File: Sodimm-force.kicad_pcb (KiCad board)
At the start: 2 copper layers, 71.6 x 71.6 mm, 1 part

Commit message: Схема закончена, часть компонентов расставлена на плате
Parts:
- removed G***: LOGO, LOGO
- added C1: 22uF, Capacitor_SMD:C_0402_1005Metric, F.Cu at (151.9, 58.5)
- added C10: 22uF, Capacitor_SMD:C_0402_1005Metric, F.Cu at (154.8, 64.4)
- added C11: 22uF, Capacitor_SMD:C_0402_1005Metric, F.Cu at (154.8, 66.4)
- added C12: 22uF, Capacitor_SMD:C_0402_1005Metric, F.Cu at (154.8, 68.3)
- added C13: 100nF, Capacitor_SMD:C_0402_1005Metric, F.Cu at (157.7, 58.5)
- added C14: 100nF, Capacitor_SMD:C_0402_1005Metric, F.Cu at (157.7, 60.5)
- added C15: 100nF, Capacitor_SMD:C_0402_1005Metric, F.Cu at (157.7, 62.4)
- added C16: 100nF, Capacitor_SMD:C_0402_1005Metric, F.Cu at (157.7, 64.4)
- added C17: 100nF, Capacitor_SMD:C_0402_1005Metric, F.Cu at (157.7, 66.4)
- added C18: 100nF, Capacitor_SMD:C_0402_1005Metric, F.Cu at (157.7, 68.3)
- added C19: 22uF, Capacitor_SMD:C_0402_1005Metric, F.Cu at (160.5, 58.5)
- added C2: 22uF, Capacitor_SMD:C_0402_1005Metric, F.Cu at (151.9, 60.5)
- added C20: 22uF, Capacitor_SMD:C_0402_1005Metric, F.Cu at (160.5, 60.5)
- added C21: 22uF, Capacitor_SMD:C_0402_1005Metric, F.Cu at (160.5, 62.4)
- added C22: 22uF, Capacitor_SMD:C_0402_1005Metric, F.Cu at (160.5, 64.4)
- added C23: 100nF, Capacitor_SMD:C_0402_1005Metric, F.Cu at (138.8, 74.5)
- added C24: 100nF, Capacitor_SMD:C_0402_1005Metric, F.Cu at (138.8, 76.5)
- added C25: 10uF, Capacitor_SMD:C_0402_1005Metric, F.Cu at (138.8, 78.5)
- added C26: 100nF, Capacitor_SMD:C_0402_1005Metric, F.Cu at (138.8, 80.4)
- added C27: 2.2uF, Capacitor_SMD:C_0402_1005Metric, F.Cu at (138.8, 82.4)
- added C28: 100nF, Capacitor_SMD:C_0402_1005Metric, F.Cu at (138.8, 84.4)
- added C29: 10uF, Capacitor_SMD:C_0402_1005Metric, F.Cu at (138.8, 86.3)
- added C3: 22uF, Capacitor_SMD:C_0402_1005Metric, F.Cu at (151.9, 62.4)
- added C30: 2.2uF, Capacitor_SMD:C_0402_1005Metric, F.Cu at (141.6, 74.5)
- added C31: 1nF, Capacitor_SMD:C_0402_1005Metric, F.Cu at (141.6, 76.5)
- added C32: 100nF, Capacitor_SMD:C_0402_1005Metric, F.Cu at (141.6, 78.5)
- added C33: 22uF, Capacitor_SMD:C_0402_1005Metric, F.Cu at (141.6, 80.4)
- added C34: 2.2uF, Capacitor_SMD:C_0402_1005Metric, F.Cu at (141.6, 82.4)
- added C35: 12p, Capacitor_SMD:C_0402_1005Metric, F.Cu at (141.6, 84.4)
- added C36: 2.2uF, Capacitor_SMD:C_0402_1005Metric, F.Cu at (141.6, 86.3)
- added C37: 220nF, Capacitor_SMD:C_0402_1005Metric, F.Cu at (144.5, 74.5)
- added C38: 22uF, Capacitor_SMD:C_0402_1005Metric, F.Cu at (144.5, 76.5)
- added C39: 220nF, Capacitor_SMD:C_0402_1005Metric, F.Cu at (144.5, 78.5)
- added C4: 22uF, Capacitor_SMD:C_0402_1005Metric, F.Cu at (151.9, 64.4)
- added C40: 2.2uF, Capacitor_SMD:C_0402_1005Metric, F.Cu at (144.5, 80.4)
- added C41: 22uF, Capacitor_SMD:C_0402_1005Metric, F.Cu at (144.5, 82.4)
- added C42: 12p, Capacitor_SMD:C_0402_1005Metric, F.Cu at (144.5, 84.4)
- added C43: 2.2uF, Capacitor_SMD:C_0402_1005Metric, F.Cu at (144.5, 86.3)
- added C44: 22uF, Capacitor_SMD:C_0402_1005Metric, F.Cu at (147.4, 74.5)
- added C45: 2.2uF, Capacitor_SMD:C_0402_1005Metric, F.Cu at (147.4, 76.5)
- added C46: 220nF, Capacitor_SMD:C_0402_1005Metric, F.Cu at (147.4, 78.5)
- added C47: 22uF, Capacitor_SMD:C_0402_1005Metric, F.Cu at (147.4, 80.4)
- added C48: 2.2uF, Capacitor_SMD:C_0402_1005Metric, F.Cu at (147.4, 82.4)
- added C49: 22uF, Capacitor_SMD:C_0402_1005Metric, F.Cu at (147.4, 84.4)
- added C5: 22uF, Capacitor_SMD:C_0402_1005Metric, F.Cu at (151.9, 66.4)
- added C50: 1uF, Capacitor_SMD:C_0402_1005Metric, F.Cu at (147.4, 86.3)
- added C51: 2.2uF, Capacitor_SMD:C_0402_1005Metric, F.Cu at (150.3, 74.5)
- added C52: 10uF, Capacitor_SMD:C_0402_1005Metric, F.Cu at (150.3, 76.5)
- added C53: 22uF, Capacitor_SMD:C_0402_1005Metric, F.Cu at (150.3, 78.5)
- added C54: 2.2uF, Capacitor_SMD:C_0402_1005Metric, F.Cu at (150.3, 80.4)
- added C55: 22uF, Capacitor_SMD:C_0402_1005Metric, F.Cu at (150.3, 82.4)
- added C56: 2.2uF, Capacitor_SMD:C_0402_1005Metric, F.Cu at (150.3, 84.4)
- added C57: 1uF, Capacitor_SMD:C_0402_1005Metric, F.Cu at (150.3, 86.3)
- added C58: 2.2uF, Capacitor_SMD:C_0402_1005Metric, F.Cu at (153.1, 74.5)
- added C59: 1uF, Capacitor_SMD:C_0402_1005Metric, F.Cu at (153.1, 76.5)
- added C6: 22uF, Capacitor_SMD:C_0402_1005Metric, F.Cu at (151.9, 68.3)
- added C60: 2.2uF, Capacitor_SMD:C_0402_1005Metric, F.Cu at (153.1, 78.5)
- added C61: 100nF, Capacitor_SMD:C_0402_1005Metric, F.Cu at (153.1, 80.4)
- added C62: 2.2uF, Capacitor_SMD:C_0402_1005Metric, F.Cu at (153.1, 82.4)
- added C63: 1uF, Capacitor_SMD:C_0402_1005Metric, F.Cu at (153.1, 84.4)
- added C64: 22uF, Capacitor_SMD:C_0402_1005Metric, F.Cu at (105.4, 88.0)
- added C65: 2.2uF, Capacitor_SMD:C_0402_1005Metric, F.Cu at (105.4, 89.9)
- added C66: 2.2uF, Capacitor_SMD:C_0402_1005Metric, F.Cu at (105.4, 91.9)
- added C67: 2.2uF, Capacitor_SMD:C_0402_1005Metric, F.Cu at (105.4, 93.9)
- added C68: 1uF, Capacitor_SMD:C_0402_1005Metric, F.Cu at (105.4, 95.9)
- added C69: 1uF, Capacitor_SMD:C_0402_1005Metric, F.Cu at (105.4, 97.8)
- added C7: 22uF, Capacitor_SMD:C_0402_1005Metric, F.Cu at (154.8, 58.5)
- added C70: 100nF, Capacitor_SMD:C_0402_1005Metric, F.Cu at (105.4, 99.8)
- added C71: 100nF, Capacitor_SMD:C_0402_1005Metric, F.Cu at (108.3, 88.0)
- added C72: 100nF, Capacitor_SMD:C_0402_1005Metric, F.Cu at (108.3, 89.9)
- added C73: 100nF, Capacitor_SMD:C_0402_1005Metric, F.Cu at (108.3, 91.9)
- added C74: 1uF, Capacitor_SMD:C_0402_1005Metric, F.Cu at (108.3, 93.9)
- added C75: 1uF, Capacitor_SMD:C_0402_1005Metric, F.Cu at (108.3, 95.9)
- added C76: 1uF, Capacitor_SMD:C_0402_1005Metric, F.Cu at (108.3, 97.8)
- added C77: 100nF, Capacitor_SMD:C_0402_1005Metric, F.Cu at (108.3, 99.8)
- added C78: 100nF, Capacitor_SMD:C_0402_1005Metric, F.Cu at (111.1, 88.0)
- added C79: 100nF, Capacitor_SMD:C_0402_1005Metric, F.Cu at (111.1, 89.9)
- added C8: 22uF, Capacitor_SMD:C_0402_1005Metric, F.Cu at (154.8, 60.5)
- added C80: 100nF, Capacitor_SMD:C_0402_1005Metric, F.Cu at (111.1, 91.9)
- added C81: 1uF, Capacitor_SMD:C_0402_1005Metric, F.Cu at (111.1, 93.9)
- added C82: 1uF, Capacitor_SMD:C_0402_1005Metric, F.Cu at (111.1, 95.9)
- added C83: 1uF, Capacitor_SMD:C_0402_1005Metric, F.Cu at (111.1, 97.8)
- added C84: 22uF, Capacitor_SMD:C_0402_1005Metric, F.Cu at (111.1, 99.8)
- added C85: 1uF, Capacitor_SMD:C_0402_1005Metric, F.Cu at (114.0, 88.0)
- added C86: 100nF, Capacitor_SMD:C_0402_1005Metric, F.Cu at (114.0, 89.9)
- added C87: 1uF, Capacitor_SMD:C_0402_1005Metric, F.Cu at (114.0, 91.9)
- added C88: 100nF, Capacitor_SMD:C_0402_1005Metric, F.Cu at (114.0, 93.9)
- added C89: 100nF, Capacitor_SMD:C_0402_1005Metric, F.Cu at (99.1, 67.0)
- added C9: 22uF, Capacitor_SMD:C_0402_1005Metric, F.Cu at (154.8, 62.4)
- added C90: 22uF, Capacitor_SMD:C_0402_1005Metric, F.Cu at (99.1, 68.9)
- added C91: 1uF, Capacitor_SMD:C_0402_1005Metric, F.Cu at (99.1, 70.9)
- added C92: 100nF, Capacitor_SMD:C_0402_1005Metric, F.Cu at (99.1, 72.9)
- added C93: 100nF, Capacitor_SMD:C_0402_1005Metric, F.Cu at (99.1, 74.9)
- added C94: 10uF, Capacitor_SMD:C_0402_1005Metric, F.Cu at (102.0, 67.0)
- added C95: 100nF, Capacitor_SMD:C_0402_1005Metric, F.Cu at (102.0, 68.9)
- added C96: 10uF, Capacitor_SMD:C_0402_1005Metric, F.Cu at (102.0, 70.9)
- added C97: 10uF, Capacitor_SMD:C_0402_1005Metric, F.Cu at (102.0, 72.9)
- added C98: 100nF, Capacitor_SMD:C_0402_1005Metric, F.Cu at (102.0, 74.9)
- added D1: B5819WS, Diode_SMD:D_SOD-323F, F.Cu at (104.7, 77.3)
- added D2: B5819WS, Diode_SMD:D_SOD-323F, F.Cu at (104.7, 80.3)
- added D3: LED-R, LED_SMD:LED_0402_1005Metric, F.Cu at (99.3, 81.5)
- added D4: LED-R, LED_SMD:LED_0402_1005Metric, F.Cu at (99.3, 83.4)
- added D5: AZ5825-01F, ESD:AZ582501F, F.Cu at (104.6, 82.8)
- added DD1: ~, H616:H616, F.Cu at (132.1, 136.1)
- added DD2: ~, SY8843QWC:SY8843QWC, F.Cu at (104.7, 139.5)
- added DD3: ~, SY8843QWC:SY8843QWC, F.Cu at (104.7, 136.2)
- added DD4: ~, SY8843QWC:SY8843QWC, F.Cu at (104.7, 132.9)
- added DD5: ~, SY8843QWC:SY8843QWC, F.Cu at (104.7, 129.7)
- added DD6: MT53E1G32D2FW-046_AUT_B, LPDDR4:BGA200C65X80P22X12_1500X1000X114N, B.Cu at (138.8, 137.3)
- added HG1: ~, IPS_ST7735_0_96:ST7735 0.96, B.Cu at (134.3, 114.3)
- added J1: SODIMM-200_Split, Connector_PCBEdge:SODIMM-200_2.5V_Card_edge, F.Cu at (98.3, 154.2)
- added J2: HDMI_C_1.4, Connector_Video:HDMI_Micro-D_Molex_46765-2x0x, F.Cu at (100.6, 114.3)
- added J3: Micro_SD_Card_Det2, Connector_Card:microSD_HC_Hirose_DM3AT-SF-PEJM5, B.Cu at (152.2, 136.8)
- added J4: USB_C_Receptacle_USB2.0_16P, Connector_USB:USB_C_Receptacle_G-Switch_GT-USB-7010ASV, F.Cu at (122.5, 115.5)
- added J5: USB_C_Receptacle_USB2.0_16P, Connector_USB:USB_C_Receptacle_G-Switch_GT-USB-7010ASV, F.Cu at (111.2, 115.5)
- added L1: 0.68uH, Inductor_SMD:L_Cenker_CKCS4020, F.Cu at (102.1, 142.8)
- added L2: 0.68uH, Inductor_SMD:L_Cenker_CKCS4020, F.Cu at (102.1, 137.2)
- added L3: 0.68uH, Inductor_SMD:L_Cenker_CKCS4020, F.Cu at (102.1, 131.5)
- added L4: 0.68uH, Inductor_SMD:L_Cenker_CKCS4020, F.Cu at (102.1, 125.9)
- added Q1: 2N7002, Package_TO_SOT_SMD:SOT-23, F.Cu at (100.1, 78.2)
- added R1: 10K, Resistor_SMD:R_0402_1005Metric, F.Cu at (154.6, 43.4)
- added R10: 10K, Resistor_SMD:R_0402_1005Metric, F.Cu at (157.5, 47.3)
- added R11: 8.32К, Resistor_SMD:R_0402_1005Metric, F.Cu at (157.5, 49.3)
- added R12: 10K, Resistor_SMD:R_0402_1005Metric, F.Cu at (157.5, 51.3)
- added R13: 41К, Resistor_SMD:R_0402_1005Metric, F.Cu at (157.5, 53.3)
- added R14: 9.1K, Resistor_SMD:R_0402_1005Metric, F.Cu at (157.5, 55.3)
- added R15: 16.9К, Resistor_SMD:R_0402_1005Metric, F.Cu at (160.4, 43.4)
- added R16: 10К, Resistor_SMD:R_0402_1005Metric, F.Cu at (160.4, 45.4)
- added R17: 4.7К, Resistor_SMD:R_0402_1005Metric, F.Cu at (160.4, 47.3)
- added R18: 10.2К, Resistor_SMD:R_0402_1005Metric, F.Cu at (160.4, 49.3)
- added R19: 0R, Resistor_SMD:R_0402_1005Metric, F.Cu at (138.8, 88.3)
- added R2: 10K, Resistor_SMD:R_0402_1005Metric, F.Cu at (154.6, 45.4)
- added R20: 10R, Resistor_SMD:R_0402_1005Metric, F.Cu at (138.8, 90.3)
- added R21: 10R, Resistor_SMD:R_0402_1005Metric, F.Cu at (138.8, 92.3)
- added R22: 10K, Resistor_SMD:R_0402_1005Metric, F.Cu at (138.8, 94.3)
- added R23: 10K, Resistor_SMD:R_0402_1005Metric, F.Cu at (138.8, 96.3)
- added R24: 10K, Resistor_SMD:R_0402_1005Metric, F.Cu at (141.7, 88.3)
- added R25: 10K, Resistor_SMD:R_0402_1005Metric, F.Cu at (141.7, 90.3)
- added R26: 10K, Resistor_SMD:R_0402_1005Metric, F.Cu at (141.7, 92.3)
- added R27: 100R, Resistor_SMD:R_0402_1005Metric, F.Cu at (141.7, 94.3)
- added R28: 150K, Resistor_SMD:R_0402_1005Metric, F.Cu at (141.7, 96.3)
- added R29: 6K04, Resistor_SMD:R_0402_1005Metric, F.Cu at (144.6, 88.3)
- added R3: 10K, Resistor_SMD:R_0402_1005Metric, F.Cu at (154.6, 47.3)
- added R30: 20K, Resistor_SMD:R_0402_1005Metric, F.Cu at (144.6, 90.3)
- added R31: 20K, Resistor_SMD:R_0402_1005Metric, F.Cu at (144.6, 92.3)
- added R32: 240R, Resistor_SMD:R_0402_1005Metric, F.Cu at (105.4, 101.8)
- added R33: 240R, Resistor_SMD:R_0402_1005Metric, F.Cu at (105.4, 103.8)
- added R34: 100K, Resistor_SMD:R_0402_1005Metric, F.Cu at (105.4, 105.8)
- added R35: 100K, Resistor_SMD:R_0402_1005Metric, F.Cu at (105.4, 107.7)
- added R36: 1K, Resistor_SMD:R_0402_1005Metric, F.Cu at (109.1, 72.6)
- added R37: 100R, Resistor_SMD:R_0402_1005Metric, F.Cu at (109.1, 74.6)
- added R38: 10K, Resistor_SMD:R_0402_1005Metric, F.Cu at (109.1, 76.5)
- added R39: 10K, Resistor_SMD:R_0402_1005Metric, F.Cu at (109.1, 78.5)
- added R4: 10K, Resistor_SMD:R_0402_1005Metric, F.Cu at (154.6, 49.3)
- added R40: 100R, Resistor_SMD:R_0402_1005Metric, F.Cu at (109.1, 80.5)
- added R41: 100R, Resistor_SMD:R_0402_1005Metric, F.Cu at (109.1, 82.5)
- added R42: 100R, Resistor_SMD:R_0402_1005Metric, F.Cu at (112.0, 72.6)
- added R43: 100K, Resistor_SMD:R_0402_1005Metric, F.Cu at (112.0, 74.6)
- added R44: 1.8K, Resistor_SMD:R_0402_1005Metric, F.Cu at (112.0, 76.5)
- added R45: 100K, Resistor_SMD:R_0402_1005Metric, F.Cu at (112.0, 78.5)
- added R46: 100K, Resistor_SMD:R_0402_1005Metric, F.Cu at (112.0, 80.5)
- added R47: 1.8K, Resistor_SMD:R_0402_1005Metric, F.Cu at (112.0, 82.5)
- added R48: 1.8K, Resistor_SMD:R_0402_1005Metric, F.Cu at (114.9, 72.6)
- added R49: 10K, Resistor_SMD:R_0402_1005Metric, F.Cu at (114.9, 74.6)
- added R5: 0R, Resistor_SMD:R_0402_1005Metric, F.Cu at (154.6, 51.3)
- added R50: 10K, Resistor_SMD:R_0402_1005Metric, F.Cu at (114.9, 76.5)
- added R51: 10K, Resistor_SMD:R_0402_1005Metric, F.Cu at (114.9, 78.5)
- added R52: 10K, Resistor_SMD:R_0402_1005Metric, F.Cu at (114.9, 80.5)
- added R53: 5.1K, Resistor_SMD:R_0402_1005Metric, F.Cu at (114.9, 82.5)
- added R54: 5.1K, Resistor_SMD:R_0402_1005Metric, F.Cu at (117.8, 72.6)
- added R55: 36K, Resistor_SMD:R_0402_1005Metric, F.Cu at (117.8, 74.6)
- added R56: 36K, Resistor_SMD:R_0402_1005Metric, F.Cu at (117.8, 76.5)
- added R57: 5.1K, Resistor_SMD:R_0402_1005Metric, F.Cu at (117.8, 78.5)
- added R58: 5.1K, Resistor_SMD:R_0402_1005Metric, F.Cu at (117.8, 80.5)
- added R6: 0R, Resistor_SMD:R_0402_1005Metric, F.Cu at (154.6, 53.3)
- added R7: 5.1К, Resistor_SMD:R_0402_1005Metric, F.Cu at (154.6, 55.3)
- added R8: 10K, Resistor_SMD:R_0402_1005Metric, F.Cu at (157.5, 43.4)
- added R9: 6.8К, Resistor_SMD:R_0402_1005Metric, F.Cu at (157.5, 45.4)
- added SW1: SW_Push, Button_Switch_SMD:SW_Push_1P1T_NO_Vertical_Wuerth_434133025816, F.Cu at (157.3, 130.8)
- added SW2: SW_Push, Button_Switch_SMD:SW_Push_1P1T_NO_Vertical_Wuerth_434133025816, F.Cu at (157.3, 135.6)
- added SW3: SW_Push, Button_Switch_SMD:SW_Push_1P1T_NO_Vertical_Wuerth_434133025816, F.Cu at (151.3, 135.6)
- added SW4: SW_Push, Button_Switch_SMD:SW_Push_1P1T_NO_Vertical_Wuerth_434133025816, F.Cu at (151.3, 130.8)
- added U1: SPX3819M5-L, Package_TO_SOT_SMD:SOT-23-5, F.Cu at (139.9, 64.7)
- added U2: SPX3819M5-L, Package_TO_SOT_SMD:SOT-23-5, F.Cu at (139.9, 69.3)
- added U3: SPI-EEPROM, Package_SO:SOIC-8_3.9x4.9mm_P1.27mm, F.Cu at (153.5, 142.7)
- added Y1: X322524MKB4SI, Oscillator:Oscillator_SMD_EuroQuartz_XO32-4Pin_3.2x2.5mm, F.Cu at (148.1, 89.8)
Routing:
- net SDQ2: vias 0 -> 1
- net SDQ11: vias 0 -> 1
- net SDQ1: vias 0 -> 1
- net SDQ0: vias 0 -> 1
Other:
- board size 71.6 x 71.6 mm -> 67.6 x 25.4 mm

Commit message: Пытаюсь сделать трассировку DDК
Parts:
- moved DD1 6.67 mm to (125.5, 136.5)
- moved DD6 5.39 mm to (134.2, 140.2)
- moved J1 1.93 mm to (98.0, 152.3)
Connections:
- DD1 pad L15: SDQ31 -> Net-(DD1C-SZQ)
- DD1 pad L9: Net-(DD1C-VCC_DRAM_1) -> VCC-DRAM
- DD6 pad V10: SDQSON -> SDQS0N
- DD6 pad Y10: SDQMO -> SDQM0
- R31 pad 1: Net-(DD1C-VCC_DRAM_1) -> Net-(DD1C-SZQ)
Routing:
- net SDQ16: track 0.00 -> 19.5 mm, vias 0 -> 2
- net SDQ12: track 0.00 -> 17.8 mm, vias 0 -> 2
- net SDQ14: track 0.00 -> 16.7 mm, vias 0 -> 2
- net SDQ18: track 0.00 -> 15.8 mm, vias 0 -> 2
- net SDQ9: track 0.00 -> 15.7 mm, vias 0 -> 2
- net SDQ17: track 0.00 -> 15.3 mm, vias 0 -> 2
- net SDQ30: track 0.00 -> 12.8 mm, vias 0 -> 2
- net SDQ3: track 0.00 -> 12.2 mm, vias 0 -> 2
- net SDQ6: track 0.00 -> 11.5 mm, vias 0 -> 2
- net SDQ5: track 0.00 -> 11.3 mm, vias 0 -> 2
- net SDQ7: track 0.00 -> 11.3 mm, vias 0 -> 2
- net SDQ4: track 0.00 -> 10.8 mm, vias 0 -> 2
- net SDQ1: track 0.00 -> 10.1 mm, vias 1 -> 2
- net SDQ31: track 0.00 -> 9.44 mm, vias 0 -> 2
- net SRST: vias 0 -> 2
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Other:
- outline, holes or cut-outs redrawn
- copper layers 2 -> 6

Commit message: вроде хехе чуть трассировки DDR
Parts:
- moved J1 7.74 mm to (96.1, 159.8)
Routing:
- net SDQ27: track 0.00 -> 15.4 mm
- net SDQ31: track 9.44 -> 19.4 mm
- net SDQ1: track 10.1 -> 19.3 mm
- net SDQ5: track 11.3 -> 19.9 mm
- net SDQ4: track 10.8 -> 19.4 mm
- net SDQ7: track 11.3 -> 19.3 mm
- net SDQ6: track 11.5 -> 19.3 mm
- net SDQ3: track 12.2 -> 19.4 mm
- net SDQ30: track 12.8 -> 19.3 mm
- net SDQ17: track 15.3 -> 19.4 mm
- net SDQ9: track 15.7 -> 19.5 mm
- net SDQ18: track 15.8 -> 19.4 mm
- net SDQ14: track 16.7 -> 19.5 mm
- net SDQ12: track 17.8 -> 19.5 mm
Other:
- outline, holes or cut-outs redrawn

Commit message: пу-пу-пу
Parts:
- moved J1 2.35 mm to (97.5, 161.7)
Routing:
- net SDQ19: track 0.00 -> 23.2 mm
- net SDQ8: track 0.00 -> 22.1 mm
- net SDQ23: track 0.00 -> 19.5 mm
- net SDQ20: track 0.00 -> 19.0 mm
- net SDQ22: track 0.00 -> 18.4 mm
- net SDQ21: track 0.00 -> 16.9 mm
- net SDQ11: track 0.00 -> 15.7 mm
- net SDQ26: track 0.00 -> 13.9 mm
- net SDQ0: track 0.00 -> 13.9 mm
- net SDQ25: track 0.00 -> 13.6 mm
- net SDQ28: track 0.00 -> 12.5 mm
- net SDQ2: track 0.00 -> 11.2 mm
- net SDQ31: track 19.4 -> 9.44 mm
- net SDQ1: track 19.3 -> 10.1 mm
- net SDQ5: track 19.9 -> 11.3 mm
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
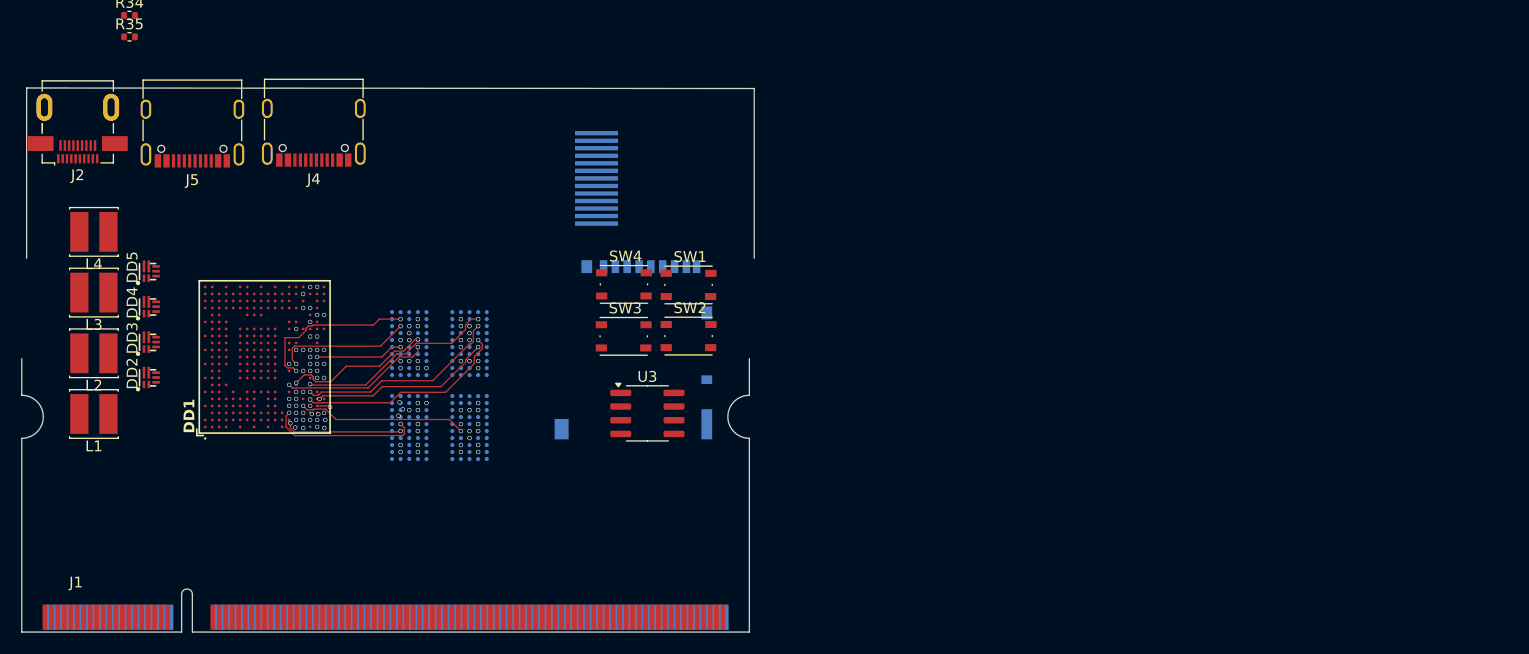
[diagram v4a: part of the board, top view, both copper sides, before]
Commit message: Добавлены предельные правила
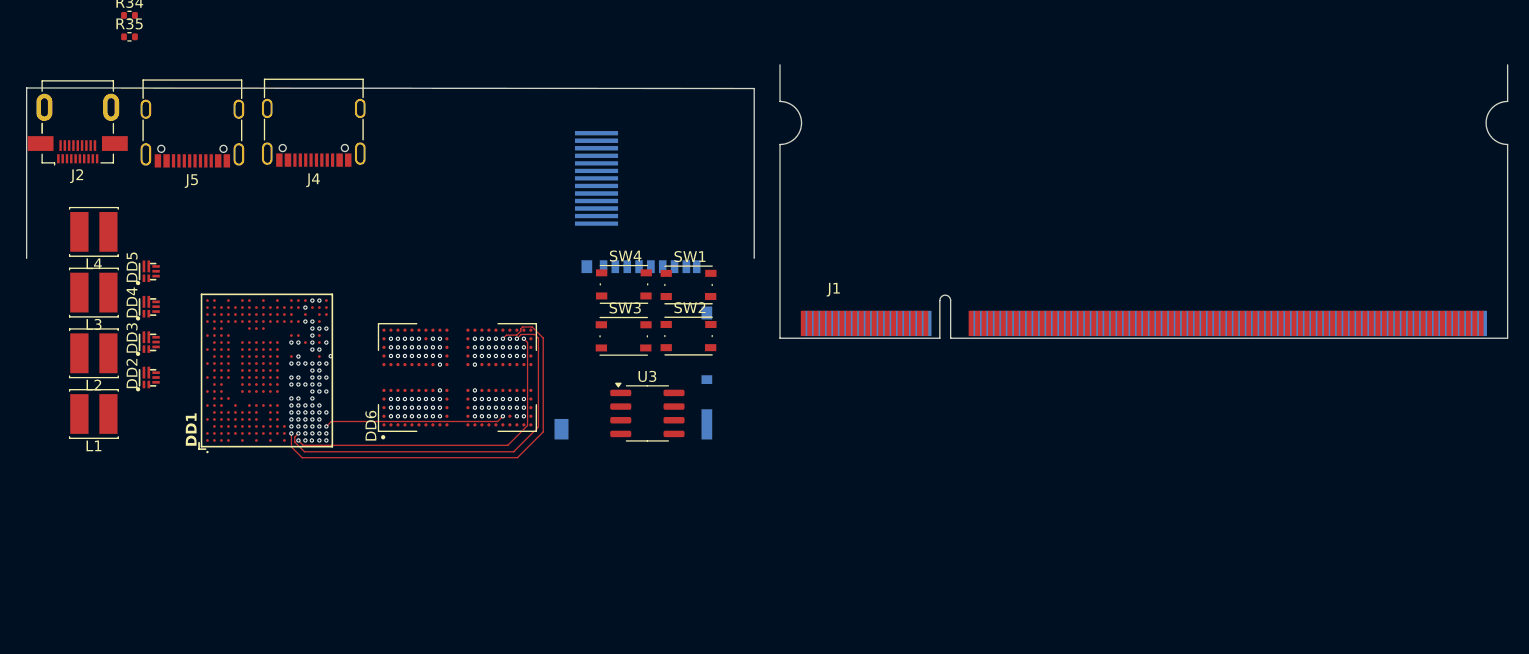
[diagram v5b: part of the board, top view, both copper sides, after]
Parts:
- DD6: moved to F.Cu
- moved J1 75.6 mm to (168.0, 134.4)
- moved DD6 1.84 mm to (135.9, 139.4), turned to 90 degrees
- moved DD1 1.28 mm to (125.7, 137.7)
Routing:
- net SDQ2: track 11.2 -> 39.5 mm
- net SDQ7: track 11.3 -> 35.5 mm
- net SDQ19: track 23.2 -> 0.00 mm
- net SDQ8: track 22.1 -> 0.00 mm
- net SDQ23: track 19.5 -> 0.00 mm
- net SDQ16: track 19.5 -> 0.00 mm
- net SDQ5: track 11.3 -> 30.4 mm
- net SDQ20: track 19.0 -> 0.00 mm
- net SDQ22: track 18.4 -> 0.00 mm
- net SDQ12: track 17.8 -> 0.00 mm
- net SDQ21: track 16.9 -> 0.00 mm
- net SDQ14: track 16.7 -> 0.00 mm
- net SDQ18: track 15.8 -> 0.00 mm
- net SDQ11: track 15.7 -> 0.00 mm
- net SDQ27: track 15.4 -> 0.00 mm
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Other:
- copper layers 6 -> 8

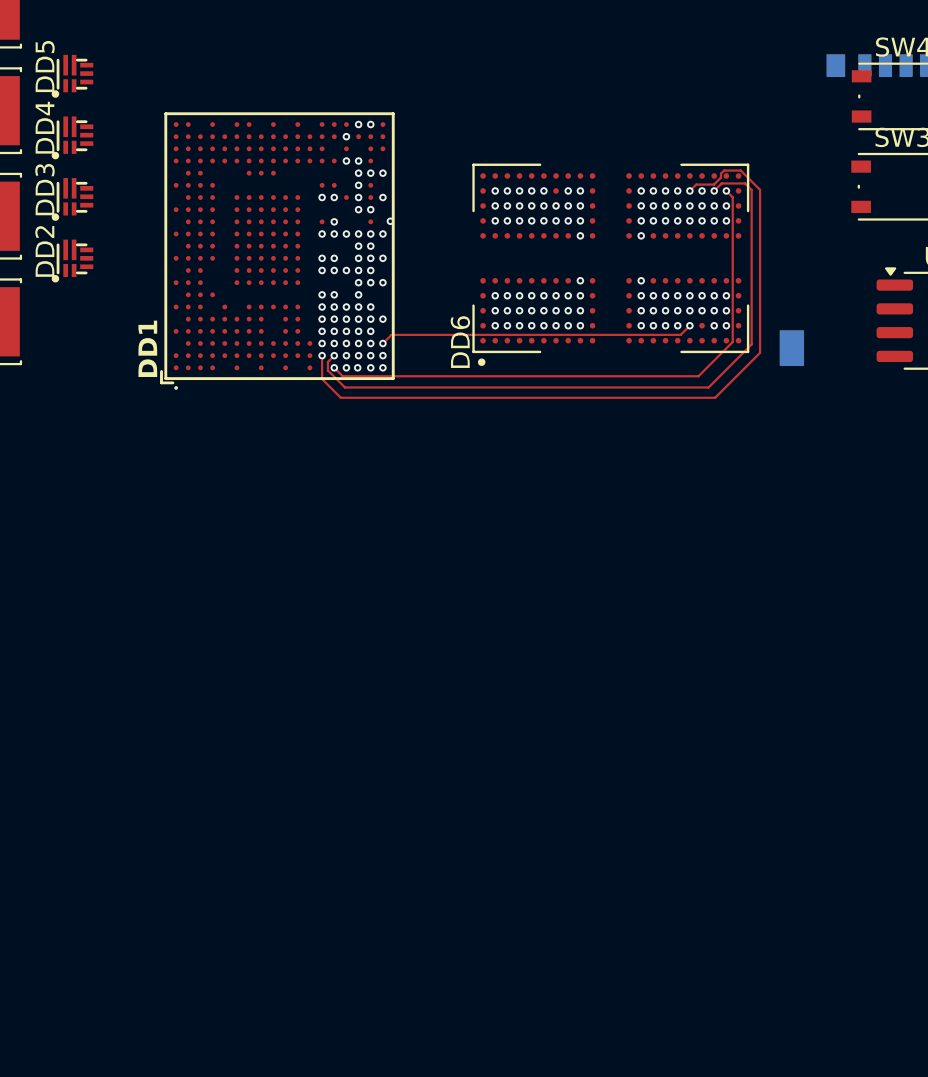
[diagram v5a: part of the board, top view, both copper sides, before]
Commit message: Трассировка с полными соединениями DDR
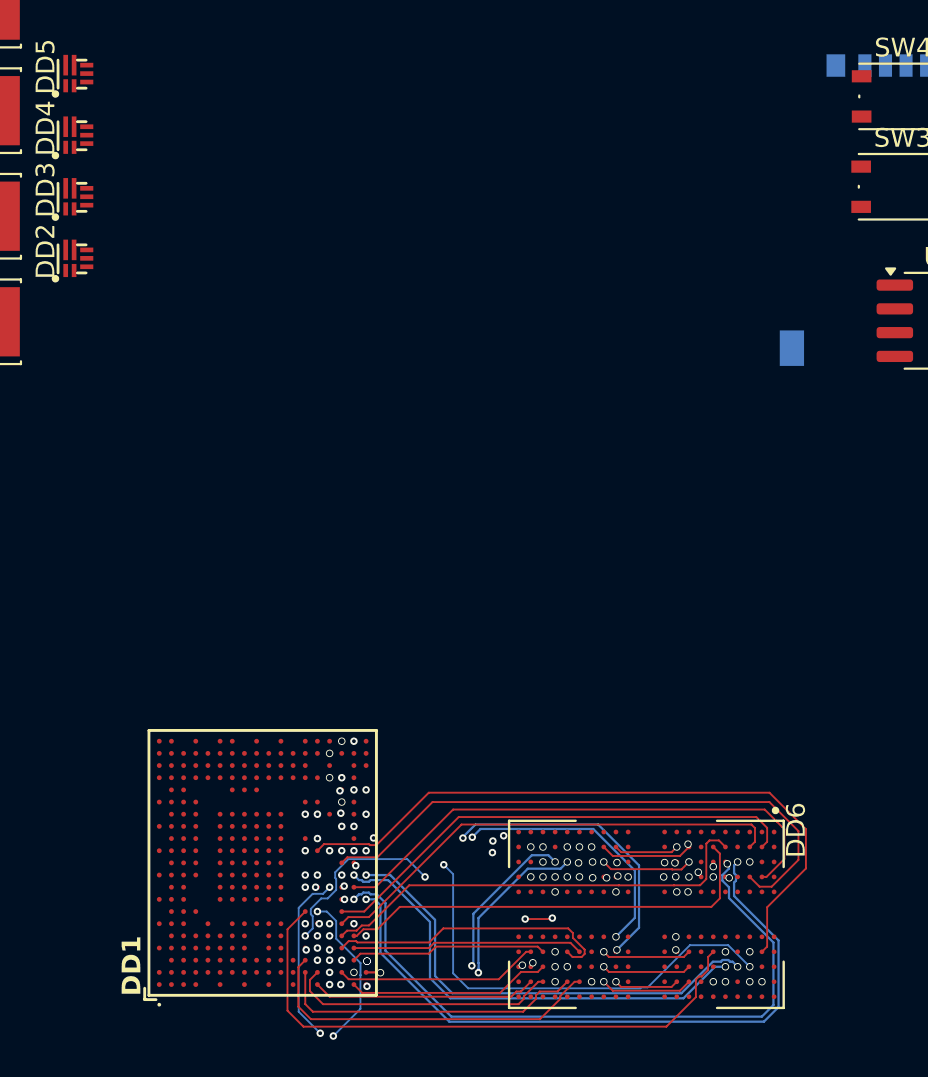
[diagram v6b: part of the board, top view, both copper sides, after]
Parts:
- moved DD6 35.1 mm to (137.8, 174.4), turned to -90 degrees
- moved DD1 33.0 mm to (124.8, 170.7)
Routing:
- net SA5: track 0.00 -> 37.5 mm, vias 3 -> 2
- net SDQS2N: track 0.00 -> 35.9 mm
- net SDQ30: track 0.00 -> 35.8 mm, vias 2 -> 0
- net SDQS2P: track 0.00 -> 35.5 mm
- net SA4: track 0.00 -> 35.0 mm, vias 3 -> 2
- net SDQ24: track 0.00 -> 34.3 mm, vias 2 -> 3
- net SDQ27: track 0.00 -> 33.6 mm
- net SRST: track 0.00 -> 33.4 mm
- net SDQ28: track 0.00 -> 32.7 mm
- net SDQ25: track 0.00 -> 31.5 mm, vias 2 -> 3
- net SDQM3: track 0.00 -> 31.5 mm, vias 2 -> 3
- net SA3: track 0.00 -> 31.4 mm, vias 3 -> 2
- net SDQ26: track 0.00 -> 31.4 mm, vias 2 -> 0
- net SDQ16: track 0.00 -> 31.3 mm, vias 2 -> 0
- net SDQ18: track 0.00 -> 30.9 mm
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
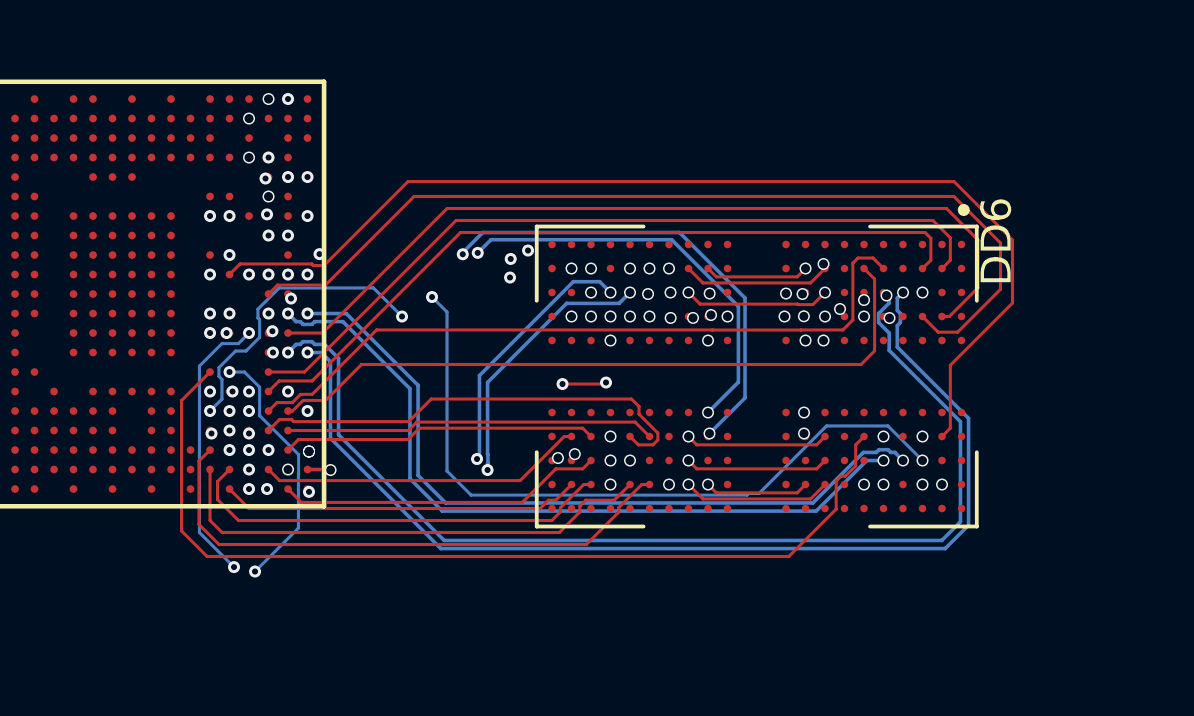
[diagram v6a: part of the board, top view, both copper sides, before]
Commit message: Согласовал по длине 1.5 слоя
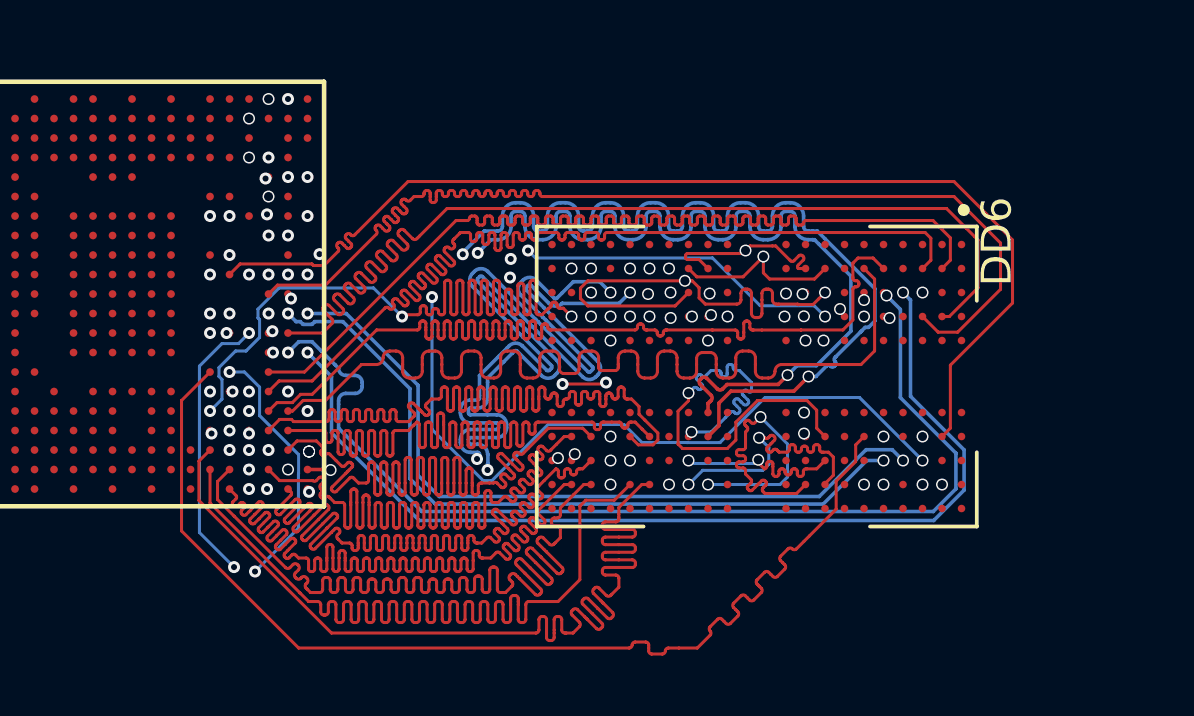
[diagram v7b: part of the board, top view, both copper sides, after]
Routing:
- net SCKE0: track 18.7 -> 70.5 mm
- net SCKE1: track 20.8 -> 51.7 mm
- net SDQ4: track 10.5 -> 36.4 mm
- net SDQ6: track 10.9 -> 36.2 mm
- net SDQM0: track 10.9 -> 36.1 mm
- net SDQ5: track 12.0 -> 36.2 mm
- net SDQ1: track 12.4 -> 36.3 mm
- net SDQ7: track 14.5 -> 36.3 mm
- net SDQ3: track 15.4 -> 36.2 mm
- net SDQ2: track 16.6 -> 36.4 mm
- net SCKP: track 24.5 -> 43.8 mm
- net SCKN: track 24.9 -> 43.7 mm
- net SDQS1N: track 14.9 -> 33.1 mm
- net SDQS1P: track 15.1 -> 33.0 mm
- net SDQ0: track 18.8 -> 36.5 mm
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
